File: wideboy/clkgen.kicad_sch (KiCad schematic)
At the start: 16 parts, among them U15 MX8350, U7 ?, U7B ?, U7C ?, Y2 14.31818M, Y3 14.705882M

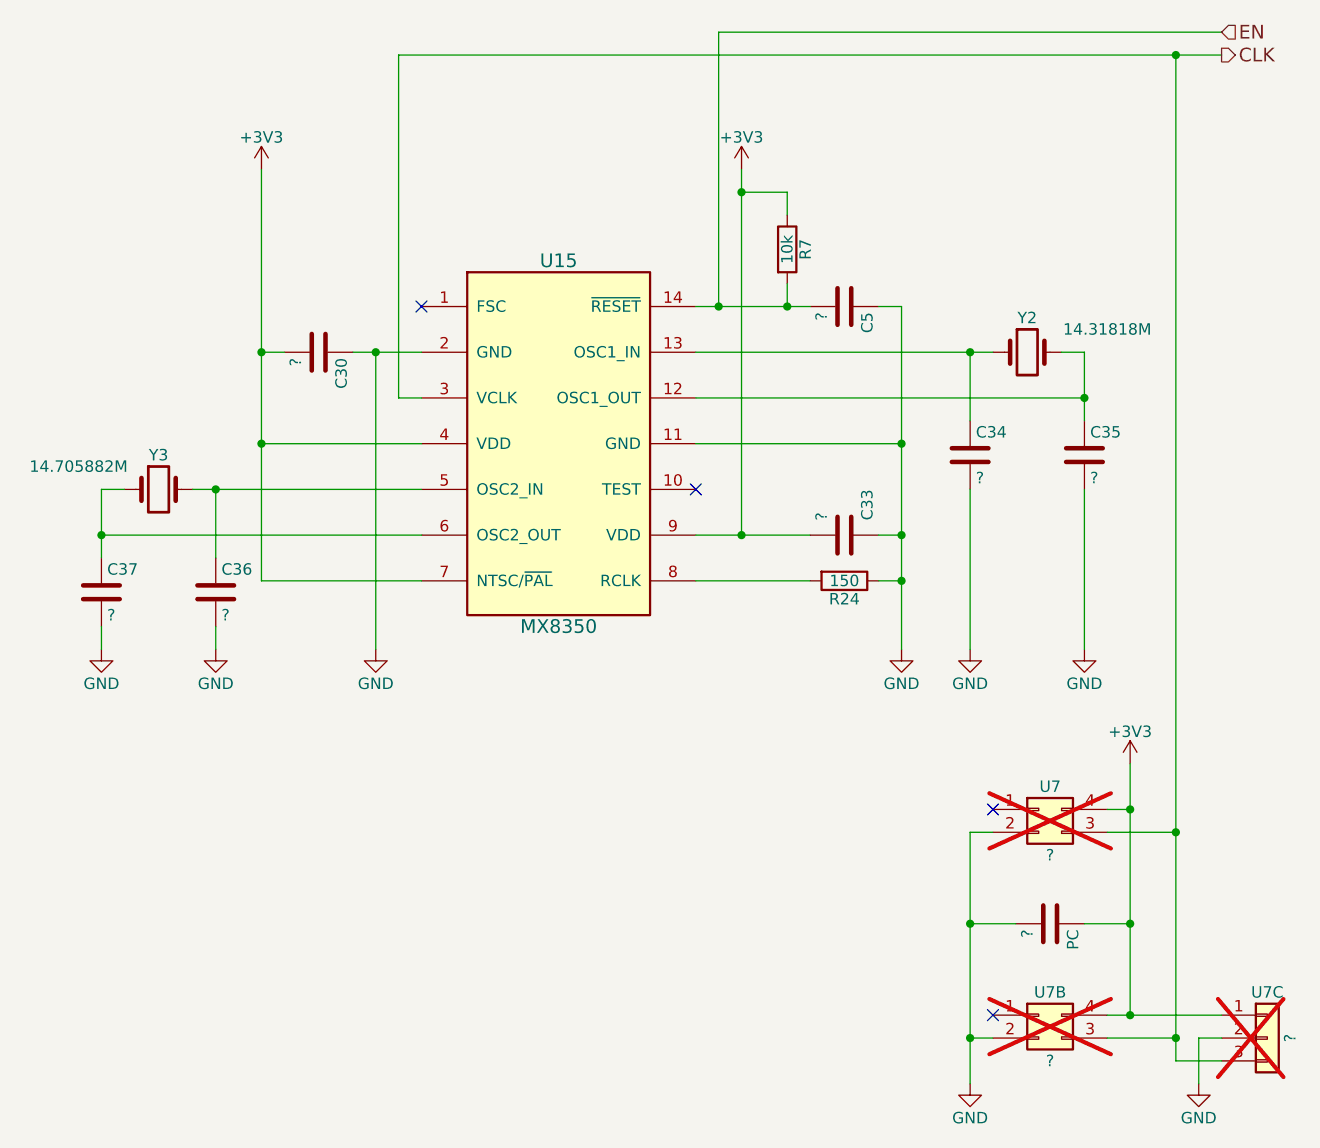
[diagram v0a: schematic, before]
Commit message: Add values for capacitors and diodes
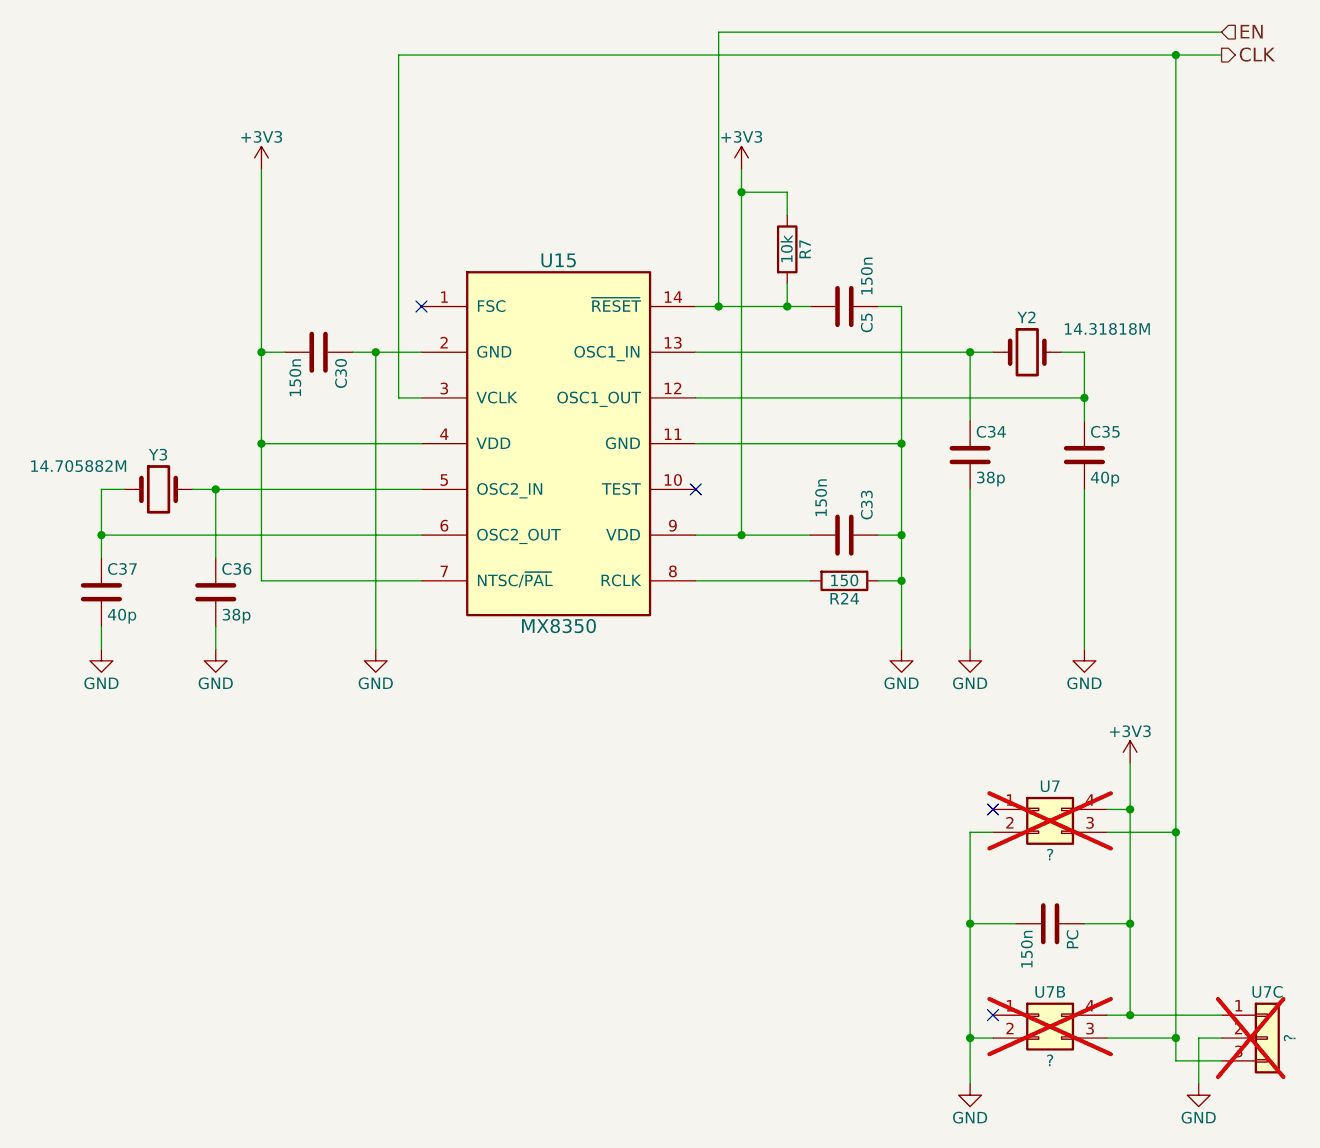
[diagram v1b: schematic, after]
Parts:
- C30, C33, C5, PC: value ? -> 150n
- C34, C36: value ? -> 38p
- C35, C37: value ? -> 40p
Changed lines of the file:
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@@
 	(title_block
 		(title "Wide-Boy64 AGB")
-		(date "2024-06-20")
-		(rev "2")
+		(date "2024-09-22")
+		(rev "3")
 		(company "CC-BY-SA-4.0 Michael Singer")
 		(comment 1 "https://github.com/msinger/wideboy/")
@@
 			)
 		)
-		(property "Value" "?"
+		(property "Value" "150n"
 			(at 102.87 74.295 0)
 			(effects
@@
 			)
 		)
-		(property "Value" "?"
+		(property "Value" "38p"
 			(at 94.615 102.87 0)
 			(effects
@@
 			)
 		)
-		(property "Value" "?"
+		(property "Value" "40p"
 			(at 81.915 102.87 0)
 			(effects
@@
 			)
 		)
-		(property "Value" "?"
+		(property "Value" "40p"
 			(at 191.135 87.63 0)
 			(effects
@@
 			)
 		)
-		(property "Value" "?"
+		(property "Value" "38p"
 			(at 178.435 87.63 0)
 			(effects
@@
 			)
 		)
-		(property "Value" "?"
-			(at 161.29 69.215 0)
+		(property "Value" "150n"
+			(at 166.37 62.992 0)
 			(effects
 				(font
@@
 			)
 		)
-		(property "Value" "?"
-			(at 161.29 91.44 0)
+		(property "Value" "150n"
+			(at 161.29 87.63 0)
 			(effects
 				(font
@@
 			)
 		)
-		(property "Value" "?"
+		(property "Value" "150n"
 			(at 184.15 137.795 0)
 			(effects
